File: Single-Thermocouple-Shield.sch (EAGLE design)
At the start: 19 parts, among them U1 TXB0104

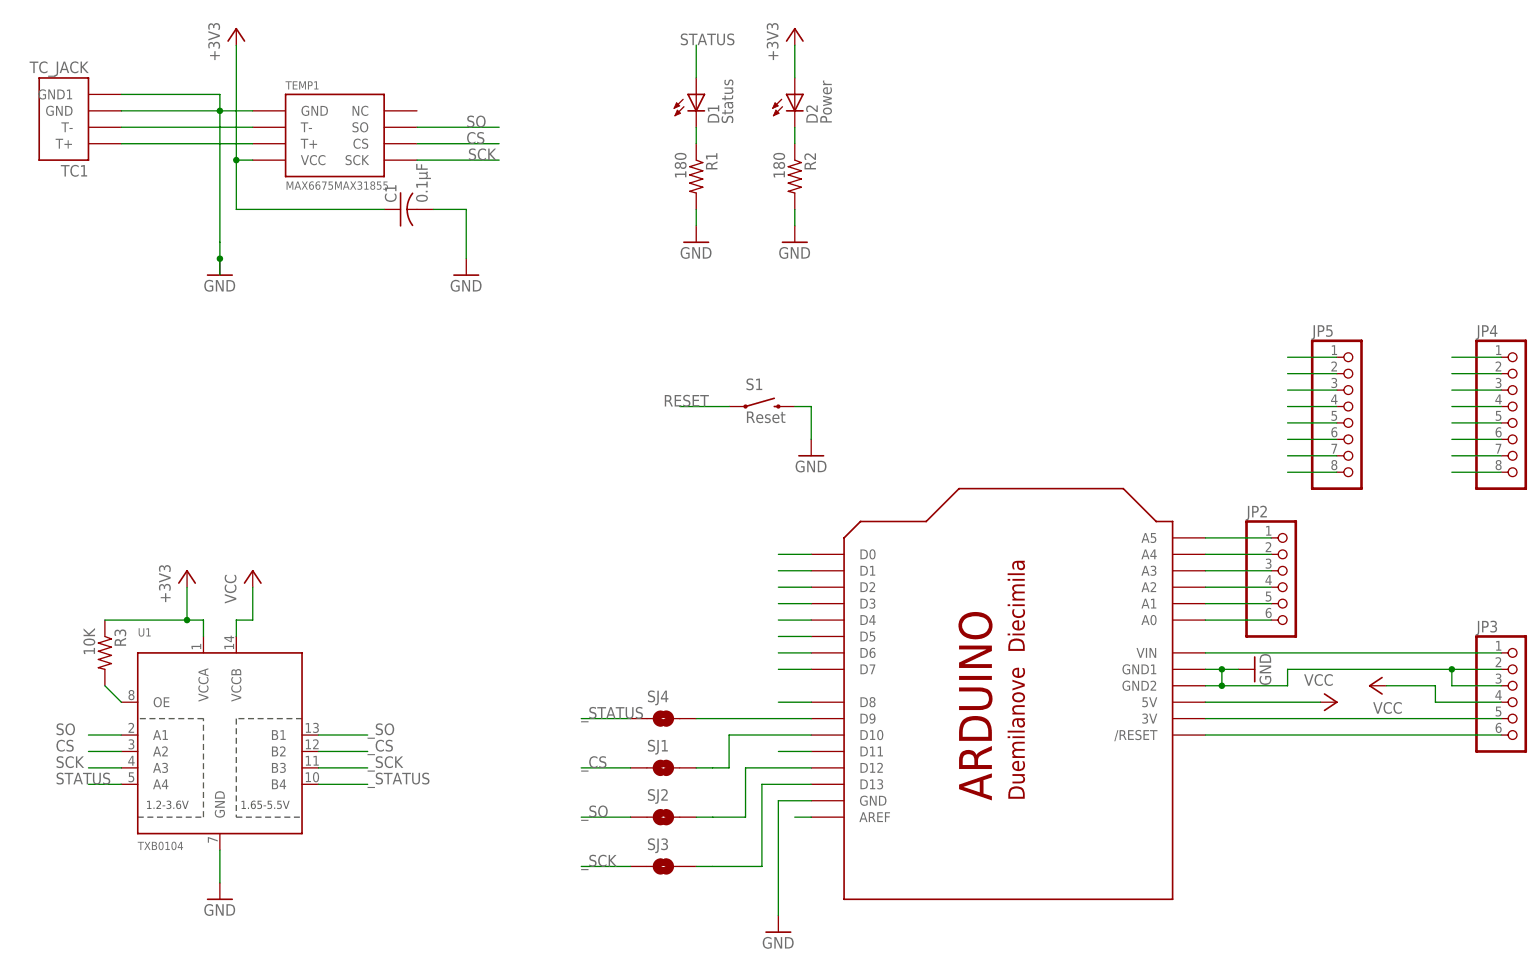
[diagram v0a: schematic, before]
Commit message: Removed routing of LED through level shifter
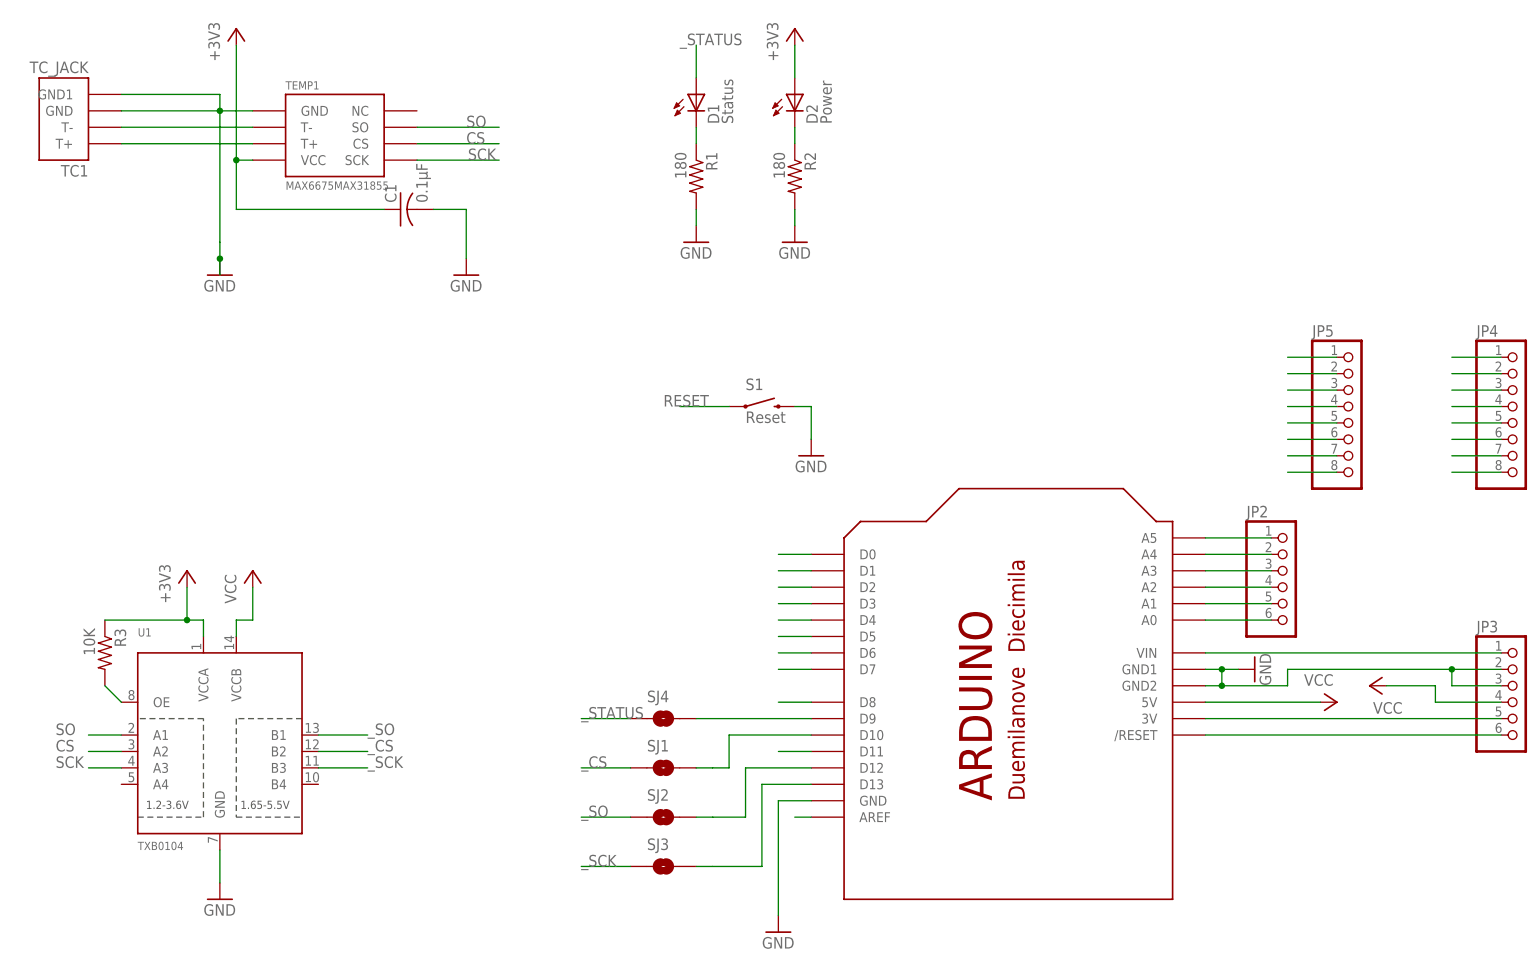
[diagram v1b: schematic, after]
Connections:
- removed net STATUS: D1.A, U1.A4
- net _STATUS: now also D1.A; no longer U1.B4
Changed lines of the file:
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@@
 </segment>
 </net>
-<net name="STATUS" class="0">
+<net name="_STATUS" class="0">
 <segment>
-<wire x1="127" y1="27.94" x2="121.92" y2="27.94" width="0.1524" layer="91"/>
-<label x="116.84" y="27.94" size="1.778" layer="95"/>
-<pinref part="U1" gate="G$1" pin="A4"/>
+<wire x1="205.74" y1="38.1" x2="198.12" y2="38.1" width="0.1524" layer="91"/>
+<label x="198.12" y="38.1" size="1.778" layer="95"/>
+<pinref part="SJ4" gate="1" pin="1"/>
 </segment>
 <segment>
@@
 </segment>
 </net>
-<net name="_STATUS" class="0">
-<segment>
-<wire x1="157.48" y1="27.94" x2="165.1" y2="27.94" width="0.1524" layer="91"/>
-<label x="165.1" y="27.94" size="1.778" layer="95"/>
-<pinref part="U1" gate="G$1" pin="B4"/>
-</segment>
-<segment>
-<wire x1="205.74" y1="38.1" x2="198.12" y2="38.1" width="0.1524" layer="91"/>
-<label x="198.12" y="38.1" size="1.778" layer="95"/>
-<pinref part="SJ4" gate="1" pin="1"/>
-</segment>
-</net>
